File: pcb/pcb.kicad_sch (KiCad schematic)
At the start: 38 parts, among them J1 Conn_01x04_Pin, J2 Conn_01x06_Pin, U1 XIAO-ESP32-C5-DIP, U10 XIAO-ESP32-C5-DIP, U11 XIAO-ESP32-C5-DIP, U12 XIAO-ESP32-C5-DIP, U13 XIAO-ESP32-C5-DIP, U14 XIAO-ESP32-C5-DIP, U15 XIAO-ESP32-C5-DIP, U17 AP2112K-3.3, U18 XIAO-ESP32-C5-DIP, U2 XIAO-ESP32-C5-DIP, U3 XIAO-ESP32-C5-DIP, U4 XIAO-ESP32-C5-DIP, U5 XIAO-ESP32-C5-DIP, U6 XIAO-ESP32-C5-DIP, U7 XIAO-ESP32-C5-DIP, U8 XIAO-ESP32-C5-DIP, U9 XIAO-ESP32-C5-DIP

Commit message: more progress with the PCB layout
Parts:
- BT1: footprint Connector_PinHeader_2.54mm:PinHeader_1x02_P2.54mm_Horizontal -> Connector_PinHeader_2.54mm:PinHeader_1x02_P2.54mm_Vertical
- J1: footprint Connector_PinHeader_2.54mm:PinHeader_1x04_P2.54mm_Horizontal -> Connector_PinHeader_2.54mm:PinHeader_1x04_P2.54mm_Vertical
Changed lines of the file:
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@@
 			)
 		)
-		(property "Footprint" "Connector_PinHeader_2.54mm:PinHeader_1x04_P2.54mm_Horizontal"
+		(property "Footprint" "Connector_PinHeader_2.54mm:PinHeader_1x04_P2.54mm_Vertical"
 			(at 125.73 133.35 0)
 			(hide yes)
@@
 			)
 		)
-		(property "Footprint" "Connector_PinHeader_2.54mm:PinHeader_1x02_P2.54mm_Horizontal"
+		(property "Footprint" "Connector_PinHeader_2.54mm:PinHeader_1x02_P2.54mm_Vertical"
 			(at 128.27 30.226 90)
 			(hide yes)

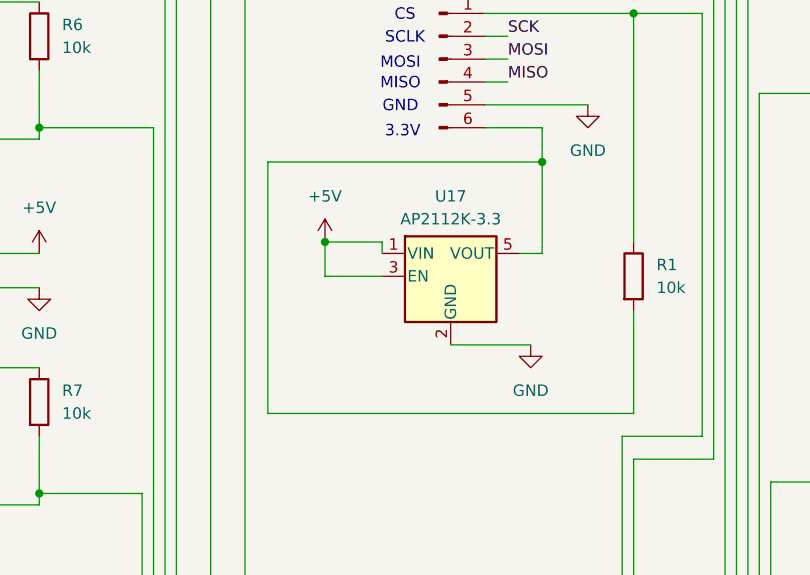
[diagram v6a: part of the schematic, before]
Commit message: swap voltage regulator for an LD1117v33 regulator
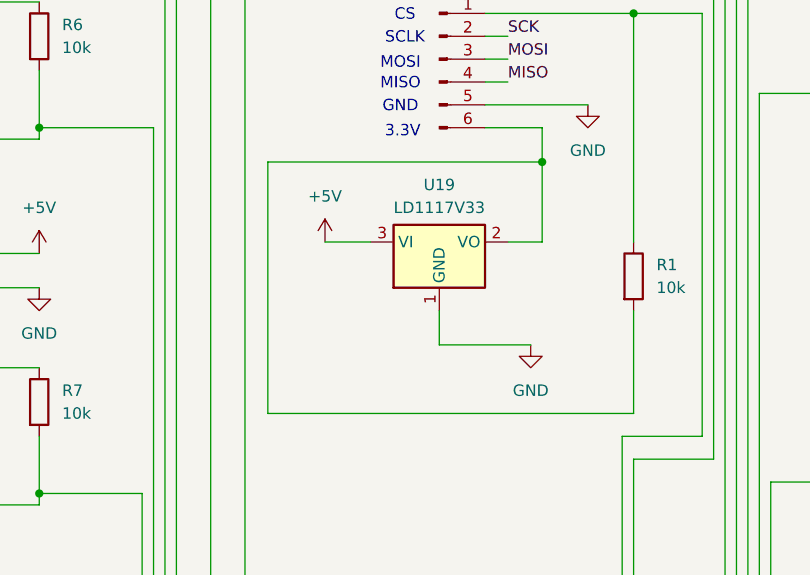
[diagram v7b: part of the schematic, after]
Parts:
- removed U17: AP2112K-3.3, Package_TO_SOT_SMD:SOT-23-5, symbol Regulator_Linear:AP2112K-3.3
- added U19: LD1117V33, Package_TO_SOT_THT:TO-220-3_Vertical, symbol Regulator_Linear:LD1117V33
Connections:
- net +5V: now also U19.3 (VI)
- net GND: now also U19.1 (GND)
- net at J2.6 (Pin_6), R1.2: now also U19.2 (VO)
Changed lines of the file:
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@@
 	)
 	(junction
-		(at 119.38 224.79)
-		(diameter 0)
-		(color 0 0 0 0)
-	)
-	(junction
 		(at 87.63 337.82)
 		(diameter 0)
@@
 	(wire
 		(pts
-			(xy 143.51 226.06) (xy 140.97 226.06)
+			(xy 143.51 224.79) (xy 139.7 224.79)
 		)
 		(stroke
@@
 	(wire
 		(pts
-			(xy 113.03 243.84) (xy 113.03 215.9)
+			(xy 113.03 215.9) (xy 113.03 243.84)
 		)
 		(stroke
@@
 	(wire
 		(pts
-			(xy 119.38 228.6) (xy 125.73 228.6)
-		)
-		(stroke
-			(width 0)
-			(type default)
-		)
-	)
-	(wire
-		(pts
 			(xy 119.38 344.17) (xy 104.14 344.17)
 		)
@@
 	(wire
 		(pts
-			(xy 143.51 215.9) (xy 143.51 226.06)
+			(xy 143.51 215.9) (xy 143.51 224.79)
 		)
 		(stroke
@@
 	(wire
 		(pts
+			(xy 132.08 236.22) (xy 142.24 236.22)
+		)
+		(stroke
+			(width 0)
+			(type default)
+		)
+	)
+	(wire
+		(pts
 			(xy 234.95 165.1) (xy 232.41 165.1)
 		)
@@
 	(wire
 		(pts
-			(xy 125.73 224.79) (xy 125.73 226.06)
-		)
-		(stroke
-			(width 0)
-			(type default)
-		)
-	)
-	(wire
-		(pts
 			(xy 21.59 173.99) (xy 87.63 173.99)
 		)
@@
 	(wire
 		(pts
-			(xy 133.35 236.22) (xy 142.24 236.22)
-		)
-		(stroke
-			(width 0)
-			(type default)
-		)
-	)
-	(wire
-		(pts
 			(xy 76.2 124.46) (xy 73.66 124.46)
 		)
@@
 	(wire
 		(pts
-			(xy 119.38 224.79) (xy 125.73 224.79)
+			(xy 119.38 224.79) (xy 124.46 224.79)
 		)
 		(stroke
@@
 	(wire
 		(pts
+			(xy 132.08 236.22) (xy 132.08 232.41)
+		)
+		(stroke
+			(width 0)
+			(type default)
+		)
+	)
+	(wire
+		(pts
 			(xy 99.06 252.73) (xy 99.06 321.31)
 		)
@@
 	(wire
 		(pts
-			(xy 119.38 224.79) (xy 119.38 228.6)
-		)
-		(stroke
-			(width 0)
-			(type default)
-		)
-	)
-	(wire
-		(pts
 			(xy 181.61 297.18) (xy 247.65 297.18)
 		)
@@
 	)
 	(symbol
+		(lib_id "Regulator_Linear:LD1117V33")
+		(at 132.08 224.79 0)
+		(unit 1)
+		(body_style 1)
+		(exclude_from_sim no)
+		(in_bom yes)
+		(on_board yes)
+		(in_pos_files yes)
+		(dnp no)
+		(fields_autoplaced yes)
+		(property "Reference" "U19"
+			(at 132.08 218.44 0)
+			(show_name no)
+			(do_not_autoplace no)
+			(effects
+				(font
+					(size 1.27 1.27)
+				)
+			)
+		)
+		(property "Value" "LD1117V33"
+			(at 132.08 220.98 0)
+			(show_name no)
+			(do_not_autoplace no)
+			(effects
+				(font
+					(size 1.27 1.27)
+				)
+			)
+		)
+		(property "Footprint" "Package_TO_SOT_THT:TO-220-3_Vertical"
+			(at 132.08 219.71 0)
+			(hide yes)
+			(show_name no)
+			(do_not_autoplace no)
+			(effects
+				(font
+					(size 1.27 1.27)
+				)
+			)
+		)
+		(property "Datasheet" "https://www.st.com/resource/en/datasheet/ld1117.pdf"
+			(at 134.62 231.14 0)
+			(hide yes)
+			(show_name no)
+			(do_not_autoplace no)
+			(effects
+				(font
+					(size 1.27 1.27)
+				)
+			)
+		)
+		(property "Description" "800 mA Fixed Low Drop Positive Voltage Regulator (ldo). Max input 15V. Fixed Output 3.3V. TO-220-3"
+			(at 132.08 224.79 0)
+			(hide yes)
+			(show_name no)
+			(do_not_autoplace no)
+			(effects
+				(font
+					(size 1.27 1.27)
+				)
+			)
+		)
+		(pin "3"
+		)
+		(pin "2"
+		)
+		(pin "1"
+		)
+		(instances
+			(project "pcb"
+				(path "/177b52ef-cce2-4dab-a936-75649664352c"
+					(reference "U19")
+					(unit 1)
+				)
+			)
+		)
+	)
+	(symbol
 		(lib_id "Connector:Conn_01x04_Pin")
 		(at 125.73 133.35 0)
@@
 					(unit 1)
 				)
-			)
-		)
-	)
-	(symbol
-		(lib_id "Regulator_Linear:AP2112K-3.3")
-		(at 133.35 228.6 0)
-		(unit 1)
-		(body_style 1)
-		(exclude_from_sim no)
-		(in_bom yes)
-		(on_board yes)
-		(in_pos_files yes)
-		(dnp no)
-		(fields_autoplaced yes)
-		(property "Reference" "U17"
-			(at 133.35 219.71 0)
-			(show_name no)
-			(do_not_autoplace no)
-			(effects
-				(font
-					(size 1.27 1.27)
-				)
-			)
-		)
-		(property "Value" "AP2112K-3.3"
-			(at 133.35 222.25 0)
-			(show_name no)
-			(do_not_autoplace no)
-			(effects
-				(font
-					(size 1.27 1.27)
-				)
-			)
-		)
-		(property "Footprint" "Package_TO_SOT_SMD:SOT-23-5"
-			(at 133.35 220.345 0)
-			(hide yes)
-			(show_name no)
-			(do_not_autoplace no)
-			(effects
-				(font
-					(size 1.27 1.27)
-				)
-			)
-		)
-		(property "Datasheet" "https://www.diodes.com/assets/Datasheets/AP2112.pdf"
-			(at 133.35 226.06 0)
-			(hide yes)
-			(show_name no)
-			(do_not_autoplace no)
-			(effects
-				(font
-					(size 1.27 1.27)
-				)
-			)
-		)
-		(property "Description" "600mA low dropout linear regulator, with enable pin, 3.8V-6V input voltage range, 3.3V fixed positive output, SOT-23-5"
-			(at 133.35 228.6 0)
-			(hide yes)
-			(show_name no)
-			(do_not_autoplace no)
-			(effects
-				(font
-					(size 1.27 1.27)
-				)
-			)
-		)
-		(pin "1"
-		)
-		(pin "2"
-		)
-		(pin "3"
-		)
-		(pin "4"
-		)
-		(pin "5"
-		)
-		(instances
-			(project "pcb"
-				(path "/177b52ef-cce2-4dab-a936-75649664352c"
-					(reference "U17")
-					(unit 1)
-				)
